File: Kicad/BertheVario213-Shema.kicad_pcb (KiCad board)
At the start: 2 copper layers, 48 x 94.5 mm, 15 parts, among them Q1 S8050, SW1 Gauche, SW2 Centre, SW3 Droit

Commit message: pcb
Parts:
- moved MS5611 9.90 mm to (143.3, 90.7), turned to 180 degrees
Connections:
- S1 pad 2: Net-(U1-5V) -> Net-(U1-Vbat)
- U1 pad 5: Net-(U1-5V) -> unconnected-(U1-5V-Pad5)
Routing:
- net Net-(GPS-NEO6M1-TX): track 93.2 -> 0.00 mm, vias 1 -> 0
- net Net-(U1-Bouton_Centre): track 0.00 -> 82.3 mm, vias 0 -> 1
- net Net-(Q1-C): track 75.7 -> 0.00 mm
- net Net-(U1-5V): track 56.6 -> 0.00 mm
- net Net-(U1-Vbat): track 28.8 -> 84.2 mm, vias 1 -> 0
- net Net-(MS5611-SCL): track 130.3 -> 104.1 mm, vias 1 -> 2
- net GNDREF: track 213.1 -> 222.8 mm, vias 1 -> 0
- net Net-(Q1-B): track 25.4 -> 18.7 mm
- net Net-(U1-Speaker): track 41.7 -> 36.5 mm
- net Net-(GPS-NEO6M1-VCC): track 147.6 -> 144.0 mm, vias 1 -> 3
- net Net-(U1-In_Vbat): track 28.9 -> 29.5 mm, vias 0 -> 1
- net Net-(MS5611-SDA): track 107.8 -> 108.0 mm, vias 2 -> 1

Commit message: pcb pb
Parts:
- Q1: footprint Package_TO_SOT_THT:TO-92_Inline -> BertheShema:S8050
- S1: value Speaker 1W 80 ohms -> Speaker 2W 8 ohms
- SW1: value Gauche -> bas
- SW2: value Centre -> milieu
- SW3: value Droit -> haut
- moved SW1 21.5 mm to (166.0, 76.0), turned to 0 degrees
- moved SW3 20.1 mm to (166.0, 96.0), turned to 0 degrees
- moved Q1 3.81 mm to (149.0, 74.3), turned to 0 degrees
- moved S1 2.50 mm to (162.5, 135.0), turned to 0 degrees
- moved QMC5883_Mag1 2.30 mm to (157.5, 150.7)
- moved SW2 1.33 mm to (166.0, 86.0), turned to 0 degrees
- moved MS5611 0.24 mm to (143.5, 90.6)
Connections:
- Q1 pad 2: Net-(Q1-C) -> Net-(Q1-B)
- Q1 pad 3: Net-(Q1-B) -> Net-(Q1-C)
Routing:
- net Net-(U1-Bouton_Centre): track 82.3 -> 0.00 mm, vias 1 -> 0
- net Net-(Q1-C): track 0.00 -> 73.0 mm
- net Net-(GPS-NEO6M1-TX): track 0.00 -> 53.1 mm, vias 0 -> 1
- net GNDREF: track 222.8 -> 198.5 mm, vias 0 -> 1
- net Net-(MS5611-SCL): track 104.1 -> 122.2 mm, vias 2 -> 1
- net Net-(MS5611-SDA): track 108.0 -> 90.1 mm, vias 1 -> 0
- net Net-(Q1-B): track 18.7 -> 26.2 mm
- net Net-(GPS-NEO6M1-VCC): track 144.0 -> 141.3 mm, vias 3 -> 1
- net Net-(U1-Speaker): track 36.5 -> 34.1 mm, vias 2 -> 0
- net Net-(U1-In_Vbat): track 29.5 -> 28.9 mm, vias 1 -> 0
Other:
- board size 48 x 94.5 mm -> 47 x 94.5 mm

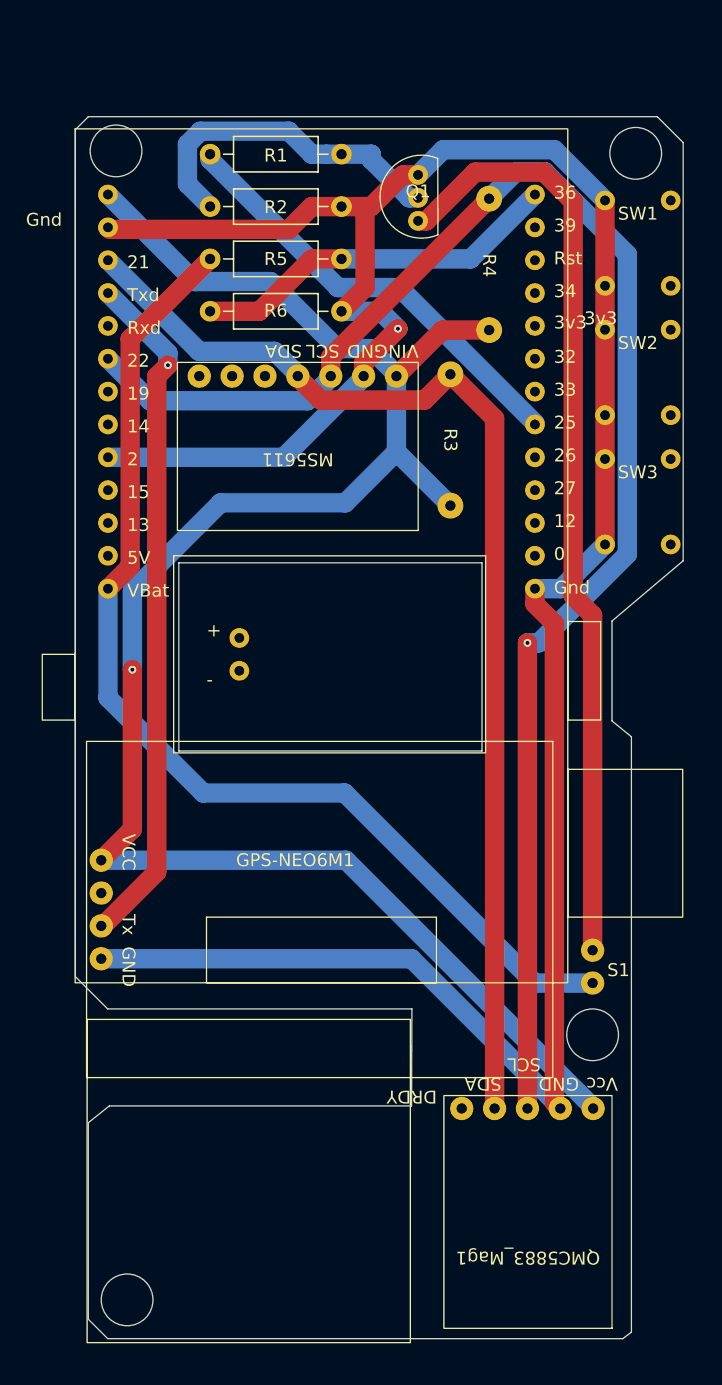
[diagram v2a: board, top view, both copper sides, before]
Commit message: pcb a verifier
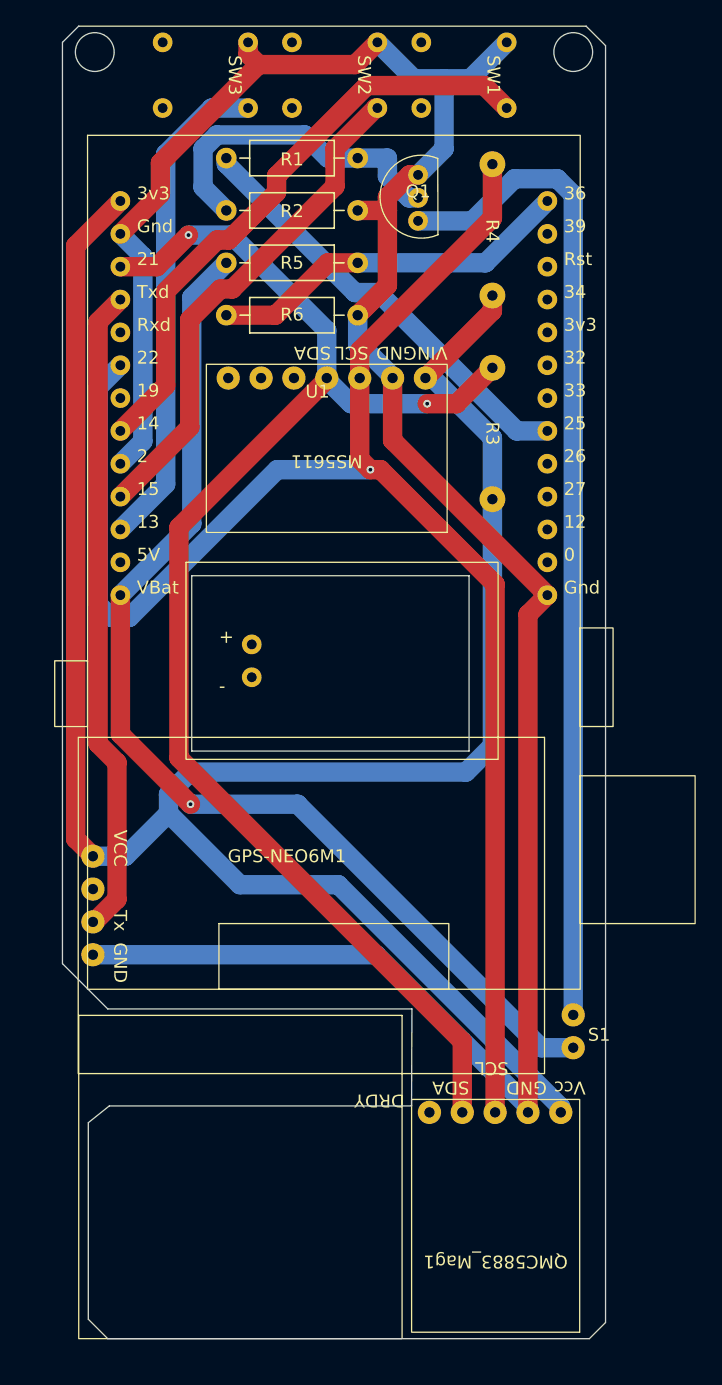
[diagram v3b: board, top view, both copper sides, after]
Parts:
- SW1: value bas -> gauche
- SW2: value milieu -> centre
- SW3: value haut -> droite
- moved SW3 44.5 mm to (134.3, 64.8), turned to -90 degrees
- moved SW2 30.3 mm to (144.3, 64.8), turned to -90 degrees
- moved SW1 16.2 mm to (154.3, 64.8), turned to -90 degrees
- moved S1 5.22 mm to (161.0, 140.0)
- moved R3 3.29 mm to (154.8, 92.5)
- moved R4 2.68 mm to (154.8, 76.8)
- moved QMC5883_Mag1 2.52 mm to (155.0, 151.0)
- moved MS5611 2.24 mm to (145.8, 90.8)
- moved R1 1.29 mm to (134.2, 71.2)
- moved R2 1.29 mm to (134.2, 75.2)
- moved R5 1.29 mm to (134.2, 79.3)
- moved R6 1.29 mm to (134.2, 83.3)
- moved U1 1.08 mm to (141.2, 89.8)
- moved GPS-NEO6M1 0.72 mm to (125.8, 129.0)
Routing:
- net Net-(U1-Bouton_Gauche): track 0.00 -> 46.7 mm
- net Net-(U1-Bouton_Centre): track 0.00 -> 38.9 mm
- net Net-(U1-Bouton_Droit): track 0.00 -> 38.3 mm
- net Net-(GPS-NEO6M1-VCC): track 141.3 -> 167.5 mm, vias 1 -> 0
- net Net-(MS5611-SDA): track 90.1 -> 109.2 mm, vias 0 -> 2
- net GNDREF: track 198.5 -> 192.2 mm, vias 1 -> 0
- net Net-(MS5611-SCL): track 122.2 -> 127.8 mm
- net Net-(Q1-C): track 73.0 -> 77.3 mm
- net Net-(GPS-NEO6M1-TX): track 53.1 -> 50.3 mm, vias 1 -> 0
- net Net-(U1-Vbat): track 83.8 -> 84.9 mm, vias 0 -> 1
- net Net-(Q1-B): track 26.2 -> 25.4 mm
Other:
- board size 47 x 94.5 mm -> 42 x 101.5 mm

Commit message: pcb a verifier
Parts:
- R1, R2, R5, R6: footprint Resistor_THT:R_Axial_DIN0207_L6.3mm_D2.5mm_P10.16mm_Horizontal -> BertheShema:R_47
- moved R1 2.75 mm to (136.9, 71.2)
- moved R2 2.75 mm to (136.9, 75.2)
- moved R5 2.75 mm to (136.9, 79.3)
- moved R6 2.75 mm to (136.9, 83.3)
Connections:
- U1 pad 13: Net-(U1-Bouton_Droit) -> (no net)
- U1 pad 14: Net-(U1-Bouton_Gauche) -> (no net)
- U1 pad 15: Net-(U1-Bouton_Centre) -> (no net)
- U1 pad 19: (no net) -> Net-(U1-Bouton_Gauche)
- U1 pad 26: (no net) -> Net-(U1-Bouton_Droit)
- U1 pad 32: (no net) -> Net-(U1-Bouton_Centre)
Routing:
- net Net-(U1-Bouton_Droit): track 38.3 -> 116.9 mm, vias 0 -> 1
- net Net-(MS5611-SCL): track 127.8 -> 107.7 mm, vias 1 -> 0
- net Net-(GPS-NEO6M1-VCC): track 167.5 -> 150.2 mm
- net GNDREF: track 192.2 -> 206.4 mm
- net Net-(MS5611-SDA): track 109.2 -> 100.3 mm
- net Net-(U1-In_Vbat): track 28.5 -> 36.1 mm, vias 0 -> 1
- net Net-(U1-Bouton_Centre): track 38.9 -> 32.4 mm
- net Net-(Q1-C): track 77.3 -> 82.6 mm, vias 0 -> 1
- net Net-(U1-Vbat): track 84.9 -> 88.8 mm, vias 1 -> 0
- net Net-(U1-Bouton_Gauche): track 46.7 -> 50.0 mm, vias 0 -> 2
- net Net-(U1-Speaker): track 33.8 -> 31.7 mm, vias 0 -> 1
- net Net-(Q1-B): track 25.4 -> 24.6 mm
